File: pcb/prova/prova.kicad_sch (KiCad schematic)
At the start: 6 parts, among them J1 Conn_01x04, U1 SN74AHCT125N

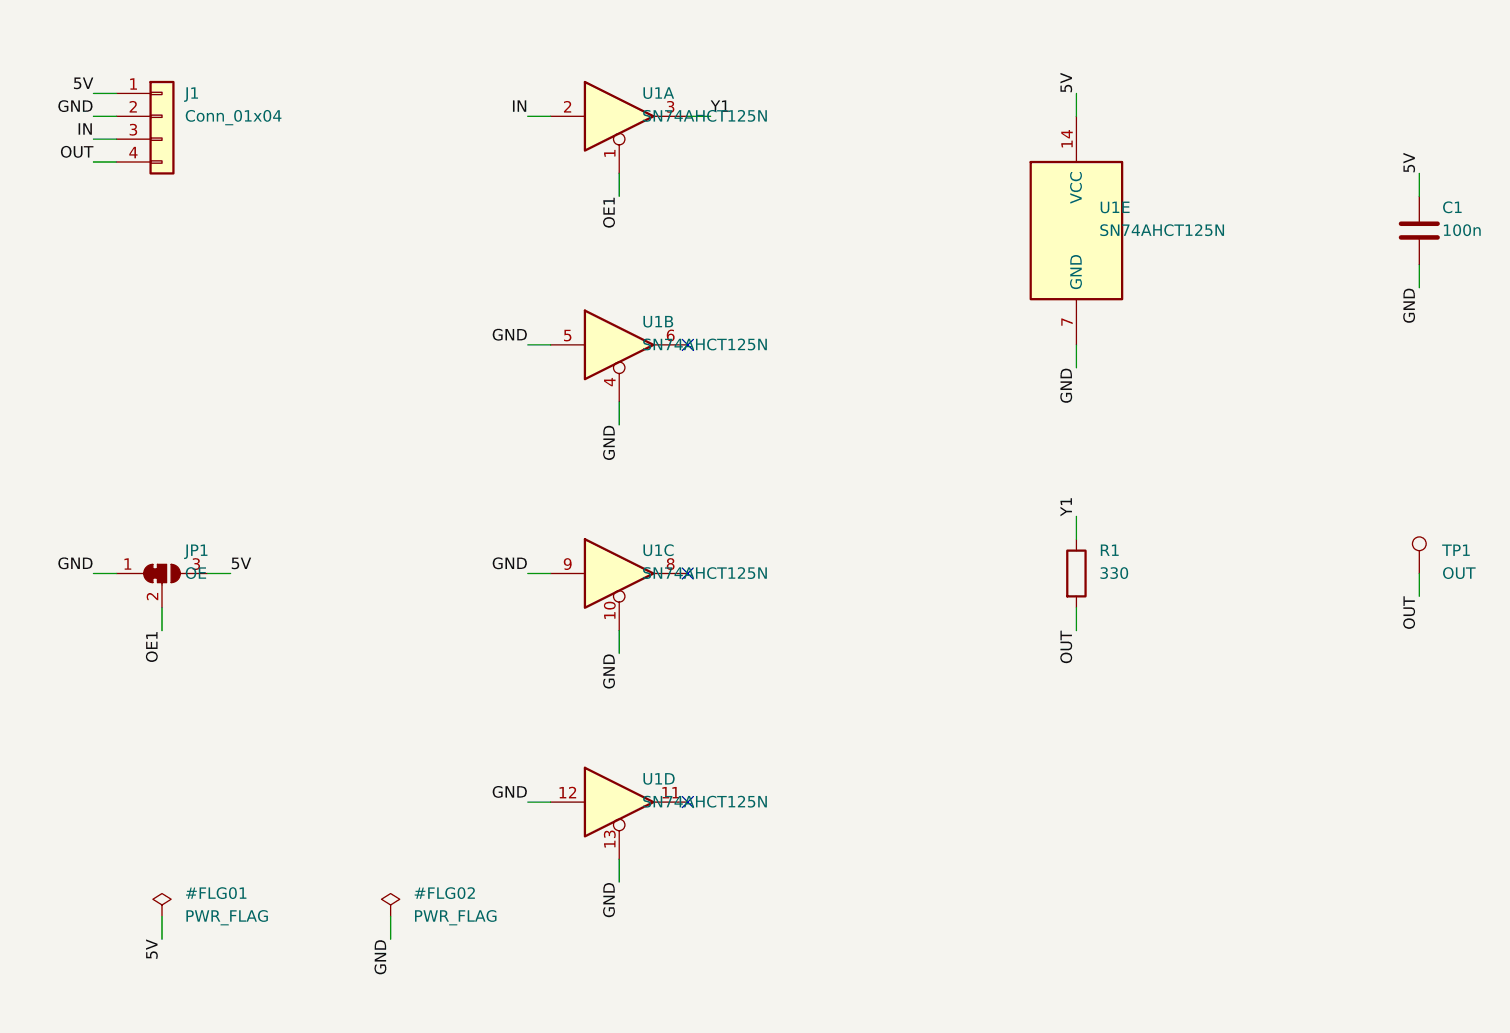
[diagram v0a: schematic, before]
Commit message: PCB, F1: regole del DRC in una fonte unica (pcb/regole/hex2.kicad_dru) copiata nei progetti da regole.py; prova con 5V_REG da 1,5 e caso di controllo delle larghezze
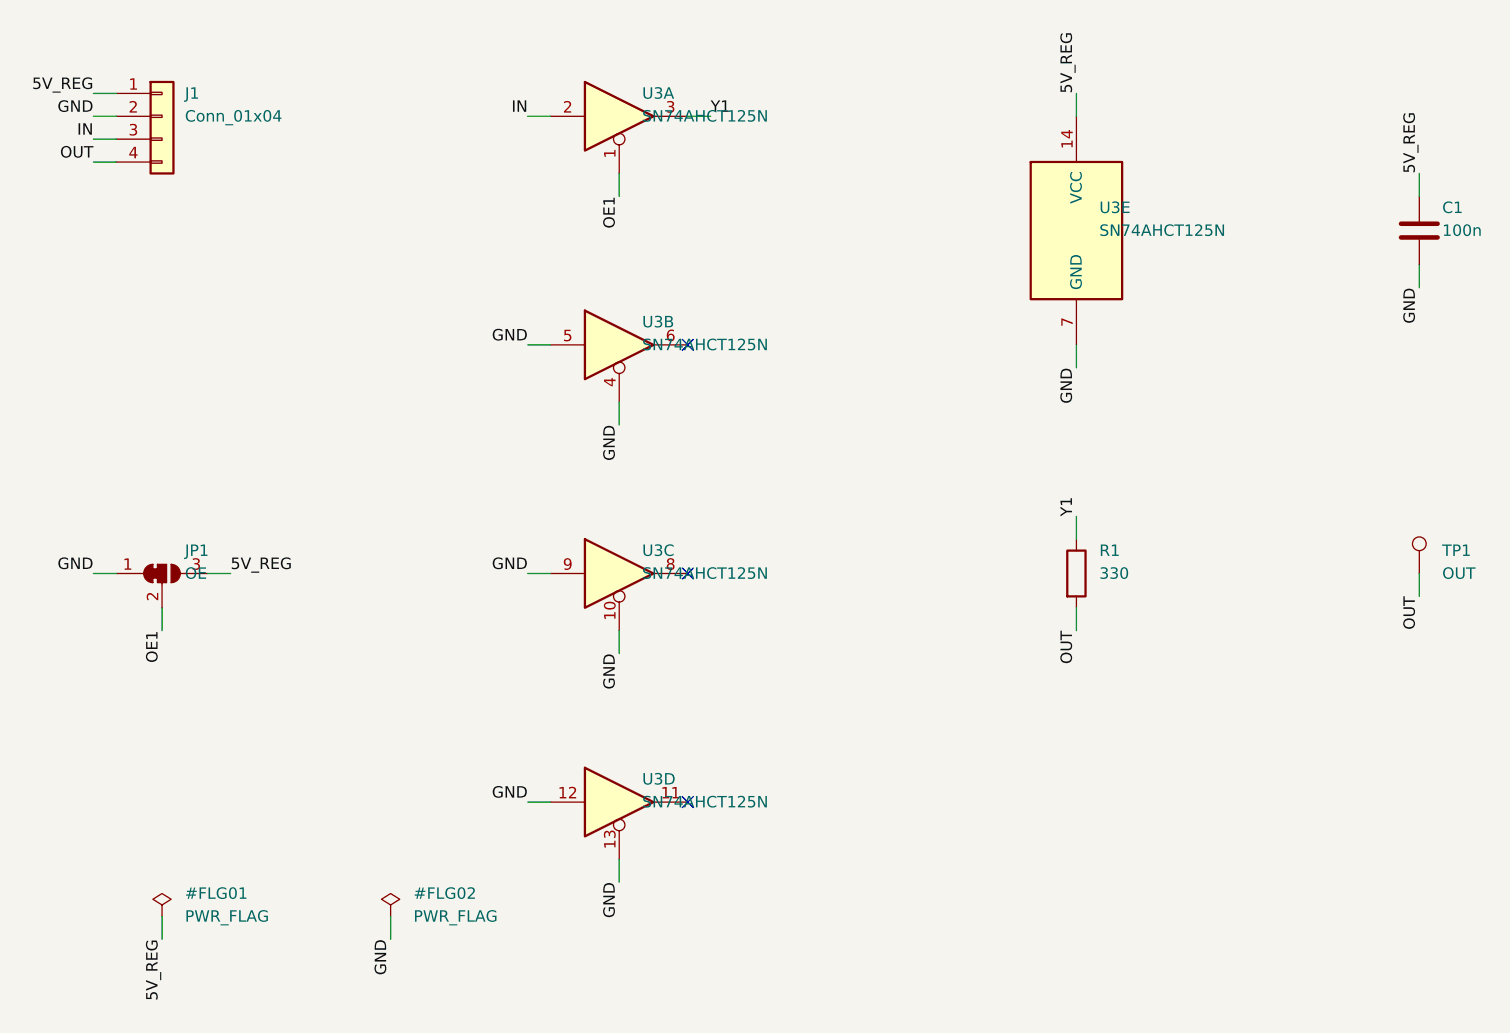
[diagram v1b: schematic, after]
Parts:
- removed U1: SN74AHCT125N, hex2:DIP-14_W7.62mm, symbol hex2_kicad:74AHCT125
- added U3: SN74AHCT125N, hex2:DIP-14_W7.62mm, symbol hex2_kicad:74AHCT125
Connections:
- net GND: now also U3.10, U3.12, U3.13, U3.4, U3.5, U3.7 (GND), U3.9
- net IN: now also U3.2
- net OE1: now also U3.1
- net Y1: now also U3.3
- net 5V renamed 5V_REG
- net 5V_REG: now also U3.14 (VCC)
